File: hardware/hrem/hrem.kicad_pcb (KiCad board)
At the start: 2 copper layers, 88.9 x 53.3 mm, 18 parts, among them J1 ICSP, J2 Hall_Conn, Q1 BC547, SW1 SW_Push_Dual, U1 HT7733A, U2 ATtiny85

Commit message: Update ICSP footprint information
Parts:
- J1: footprint Connector_PinSocket_2.54mm:PinSocket_2x05_P2.54mm_Vertical -> Connector_IDC:IDC-Header_2x05_P2.54mm_Vertical
- moved J1 5.68 mm to (63.5, 66.0)
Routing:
- net GND: track 207.6 -> 168.1 mm
- net /MOSI: track 25.5 -> 0.06 mm, vias 2 -> 0
- net /SCK: track 40.6 -> 25.4 mm
- net /MISO: track 35.6 -> 22.9 mm
- net /RST: track 10.2 -> 0.00 mm
- net VCC: track 61.0 -> 58.4 mm

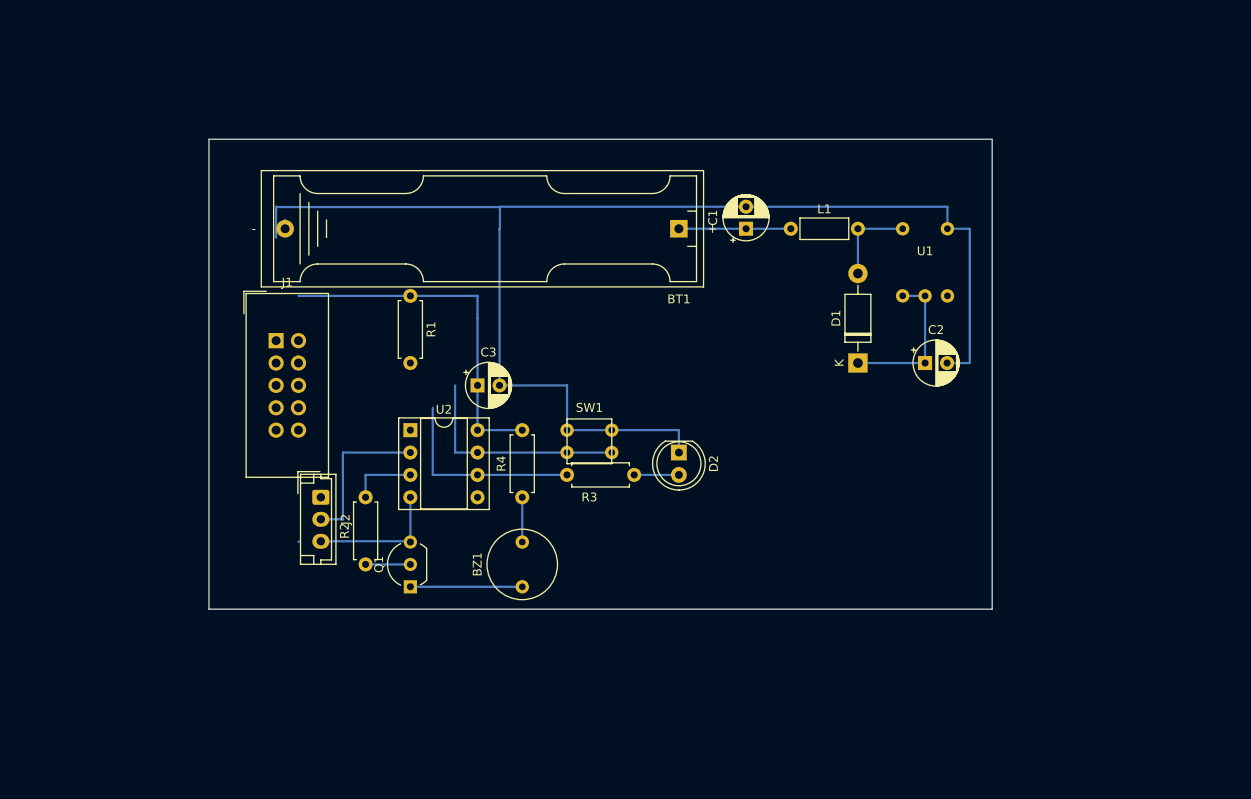
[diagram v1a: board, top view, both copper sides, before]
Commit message: KiCad new footprints
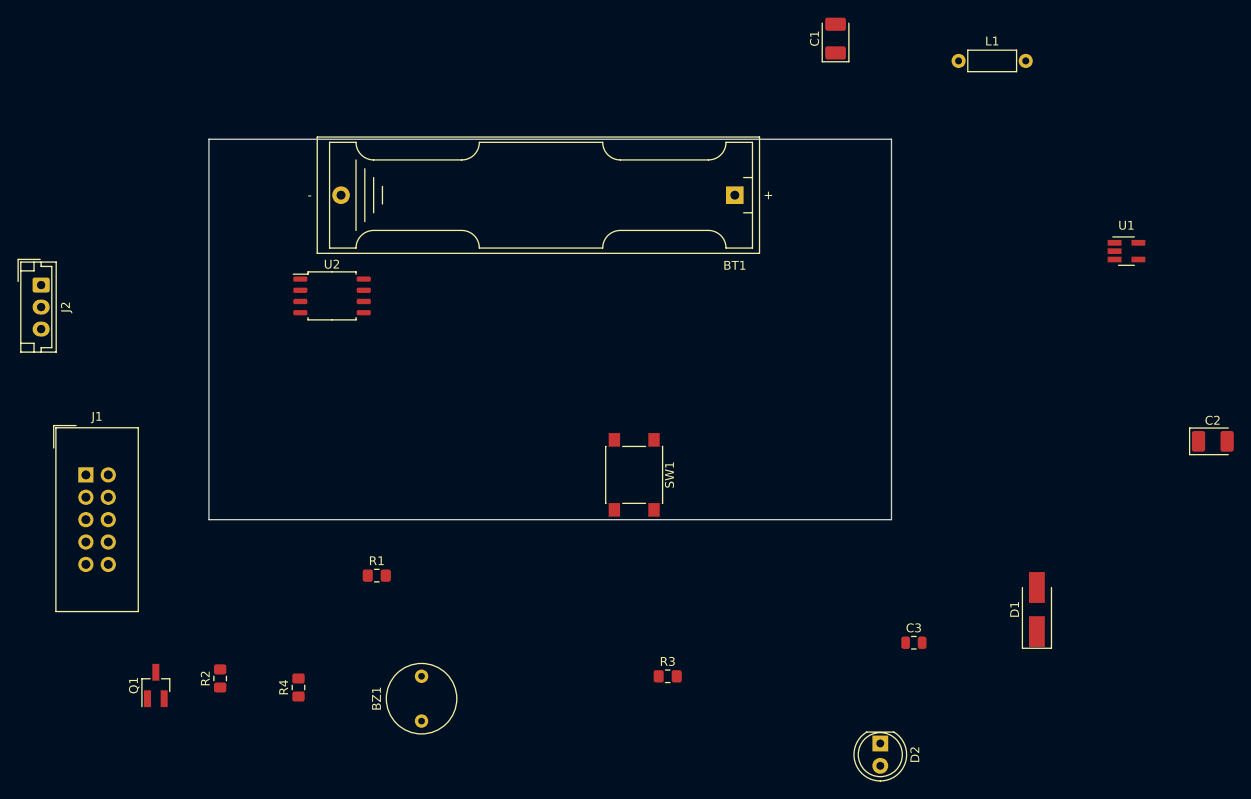
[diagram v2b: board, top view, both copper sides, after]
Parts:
- C1, C2: footprint Capacitor_THT:CP_Radial_D5.0mm_P2.50mm -> Capacitor_Tantalum_SMD:CP_EIA-3528-15_AVX-H_Pad1.50x2.35mm_HandSolder
- C3: footprint Capacitor_THT:CP_Radial_D5.0mm_P2.50mm -> Capacitor_SMD:C_0805_2012Metric
- D1: value 1N5817 -> SS14-E3/61T; footprint Diode_THT:D_DO-41_SOD81_P10.16mm_Horizontal -> Diode_SMD:D_SMA_Handsoldering
- Q1: value BC547 -> MMBT4401-7-F; footprint Package_TO_SOT_THT:TO-92_Inline_Wide -> Package_TO_SOT_SMD:SOT-23_Handsoldering
- R1, R2, R3, R4: footprint Resistor_THT:R_Axial_DIN0207_L6.3mm_D2.5mm_P7.62mm_Horizontal -> Resistor_SMD:R_0805_2012Metric_Pad1.15x1.40mm_HandSolder
- SW1: footprint hrem:button -> Button_Switch_SMD:SW_Push_1P1T_NO_6x6mm_H9.5mm
- U1: footprint hrem:HT7733 -> Package_TO_SOT_SMD:SOT-23-5_HandSoldering
- U2: footprint Package_DIP:DIP-8_W7.62mm_Socket -> Package_SO:SOIC-8_5.23x5.23mm_P1.27mm
- moved C3 57.5 mm to (135.9, 100.3)
- moved D2 40.2 mm to (132.1, 111.8)
- moved J2 39.9 mm to (36.8, 59.7)
- moved D1 34.6 mm to (149.9, 96.6)
- moved C2 33.9 mm to (169.8, 77.5)
- moved R4 33.3 mm to (66.0, 105.4)
- moved R1 32.0 mm to (74.9, 92.7), turned to 0 degrees
- moved Q1 31.0 mm to (49.9, 105.2)
- moved L1 26.9 mm to (141.0, 34.3)
- moved J1 26.4 mm to (41.9, 81.3)
- moved R3 25.6 mm to (108.0, 104.1)
- moved C1 23.9 mm to (127.0, 31.8)
- moved U1 23.4 mm to (160.0, 55.9)
- moved R2 21.0 mm to (57.1, 104.4)
- moved BZ1 19.1 mm to (80.0, 106.7)
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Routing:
- net GND: track 168.1 -> 0.00 mm
- net VCC: track 58.4 -> 0.00 mm
- net /SCK: track 25.4 -> 0.00 mm
- net /MISO: track 22.9 -> 0.00 mm
- net Net-(J2-Pad2): track 17.8 -> 0.00 mm
- net Net-(BZ1-Pad2): track 12.7 -> 0.00 mm
- net Net-(BT1-Pad1): track 12.7 -> 0.00 mm
- net Net-(D1-Pad2): track 10.2 -> 0.00 mm
- net Net-(R2-Pad2): track 7.62 -> 0.00 mm
- net Net-(BZ1-Pad1): track 5.08 -> 0.00 mm
- net Net-(Q1-Pad2): track 5.08 -> 0.00 mm
- net Net-(D2-Pad2): track 5.08 -> 0.00 mm
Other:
- board size 88.9 x 53.3 mm -> 77.5 x 43.2 mm

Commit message: Work over schematics
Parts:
- added R5: 0R, Resistor_SMD:R_0805_2012Metric_Pad1.15x1.40mm_HandSolder, F.Cu at (128.5, 61.0)
- added R6: 0R, Resistor_SMD:R_0805_2012Metric_Pad1.15x1.40mm_HandSolder, F.Cu at (123.2, 60.3)
- added REF**: KiCad-Logo2_5mm_SilkScreen, Symbol:KiCad-Logo2_5mm_SilkScreen, F.Cu at (69.2, 80.6)
- added REF**: MountingHole_3mm, MountingHole:MountingHole_3mm, F.Cu at (132.3, 46.4)
- added REF**: MountingHole_3mm, MountingHole:MountingHole_3mm, F.Cu at (132.3, 84.4)
- added REF**: MountingHole_3mm, MountingHole:MountingHole_3mm, F.Cu at (59.3, 84.4)
- added REF**: MountingHole_3mm, MountingHole:MountingHole_3mm, F.Cu at (59.3, 46.4)
- added TP1: TestPoint_Flag, TestPoint:TestPoint_Loop_D2.50mm_Drill1.0mm, F.Cu at (132.7, 57.8)
- added TP2: TestPoint_Flag, TestPoint:TestPoint_Pad_D2.0mm, F.Cu at (59.7, 77.5)
- added TP3: TestPoint_Flag, TestPoint:TestPoint_Pad_D2.0mm, F.Cu at (116.2, 72.4)
- added TP4: TestPoint_Flag, TestPoint:TestPoint_Pad_D2.0mm, F.Cu at (114.3, 83.8)
- added TP5: TestPoint_Flag, TestPoint:TestPoint_Pad_D2.0mm, F.Cu at (101.0, 81.9)
- added U3: 74LVC1G125, Package_TO_SOT_SMD:SOT-23-5_HandSoldering, F.Cu at (126.4, 70.5)
- added U4: 74LVC1G125, Package_TO_SOT_SMD:SOT-23-5_HandSoldering, F.Cu at (115.0, 62.9)
- BT1: footprint Battery:BatteryHolder_Keystone_2466_1xAAA -> hrem:AAA battery
- BZ1, SW1: moved to B.Cu
- C3: footprint Capacitor_SMD:C_0805_2012Metric -> Capacitor_SMD:C_0805_2012Metric_Pad1.15x1.40mm_HandSolder
- D2: footprint LED_THT:LED_D5.0mm -> LED_THT:LED_D3.0mm; moved to B.Cu
- J1: value ICSP -> AVR-ISP
- L1: footprint Inductor_THT:L_Axial_L5.3mm_D2.2mm_P7.62mm_Horizontal_Vishay_IM-1 -> hrem:Murata LQH43
- moved C2 99.8 mm to (71.1, 62.9)
- moved D1 95.6 mm to (59.1, 66.6)
- moved U1 94.7 mm to (66.0, 67.3)
- moved J2 88.7 mm to (123.8, 76.9)
- moved L1 82.5 mm to (62.2, 59.1)
- moved R2 81.4 mm to (127.9, 64.1), turned to 180 degrees
- moved C1 74.0 mm to (66.0, 73.7), turned to 180 degrees
- moved D2 61.3 mm to (92.7, 64.8), turned to 90 degrees
- moved R4 55.6 mm to (114.1, 77.5), turned to 0 degrees
- moved Q1 50.1 mm to (88.3, 73.0)
- moved BZ1 47.1 mm to (101.6, 64.8), turned to 90 degrees
- moved R1 41.4 mm to (114.3, 80.0)
- moved J1 40.7 mm to (82.5, 83.2), turned to 90 degrees
- moved R3 36.9 mm to (110.7, 67.3)
- moved U2 35.9 mm to (102.9, 74.9)
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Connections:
- net Net-(BT1-Pad1) renamed /Vbat
- J2 pad 1: /MOSI -> Net-(J2-Pad1)
- R3 pad 1: /MISO -> Net-(R3-Pad1)
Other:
- board size 77.5 x 43.2 mm -> 80 x 44.4 mm

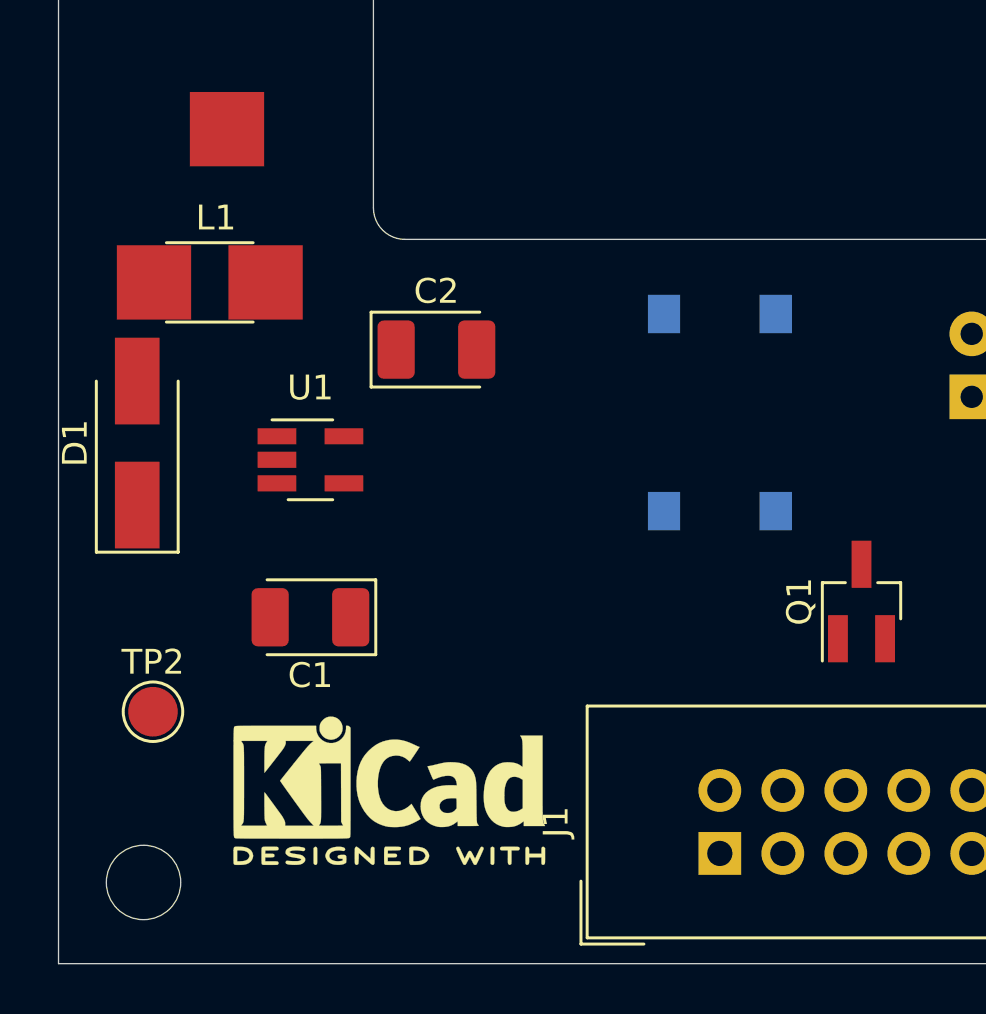
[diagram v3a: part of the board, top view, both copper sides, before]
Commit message: Button footprint added
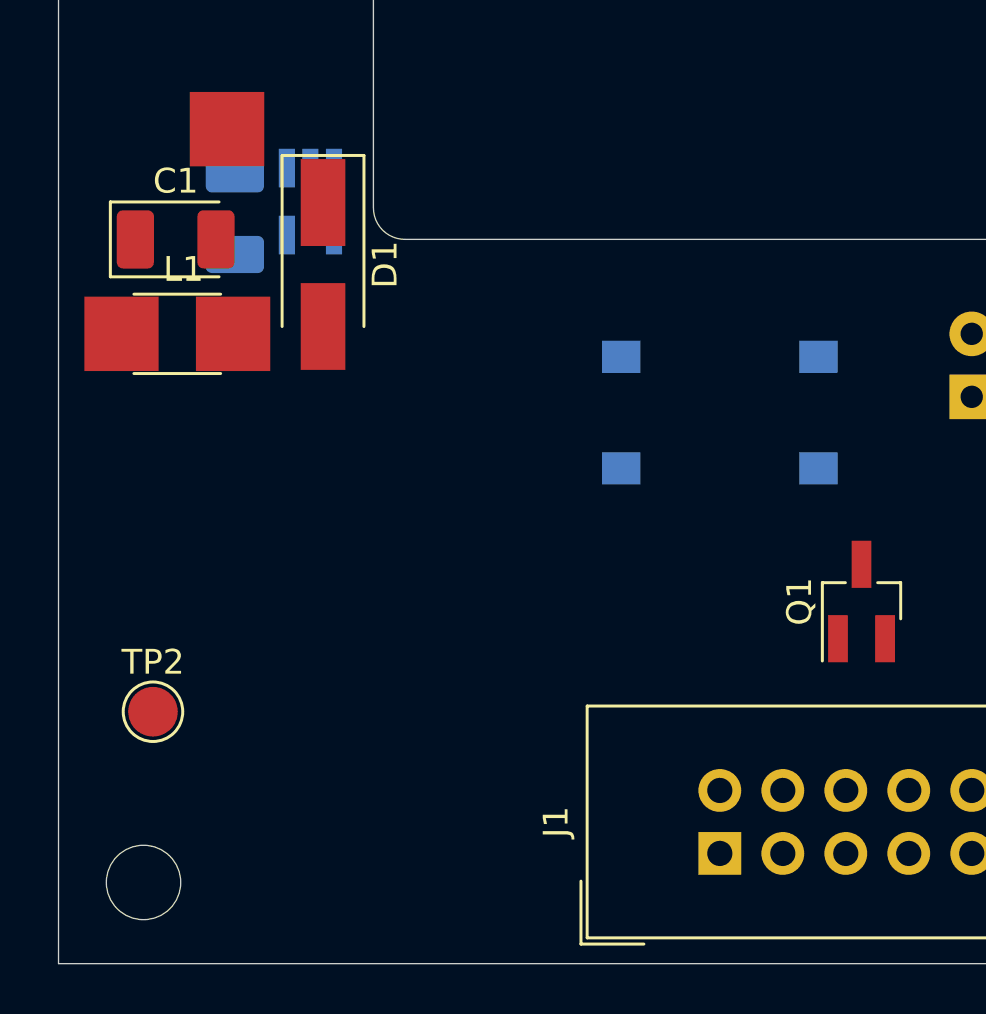
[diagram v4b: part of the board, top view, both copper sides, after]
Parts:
- removed the REF** at (69.2, 80.6)
- C2, U1: moved to B.Cu
- SW1: footprint Button_Switch_SMD:SW_Push_1P1T_NO_6x6mm_H9.5mm -> hrem:Diptronics DTSM-65N
- moved C1 16.2 mm to (60.6, 58.4), turned to 0 degrees
- moved U1 10.4 mm to (66.0, 56.9), turned to 270 degrees
- moved D1 10.4 mm to (66.5, 59.4), turned to 270 degrees
- moved C2 9.79 mm to (63.0, 57.4), turned to 270 degrees
- moved L1 2.45 mm to (60.9, 61.1)
- turned SW1 to 0 degrees
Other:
- net class POWER added: clearance 0.2, trace_width 1, via_dia 0.8, via_drill 0.4

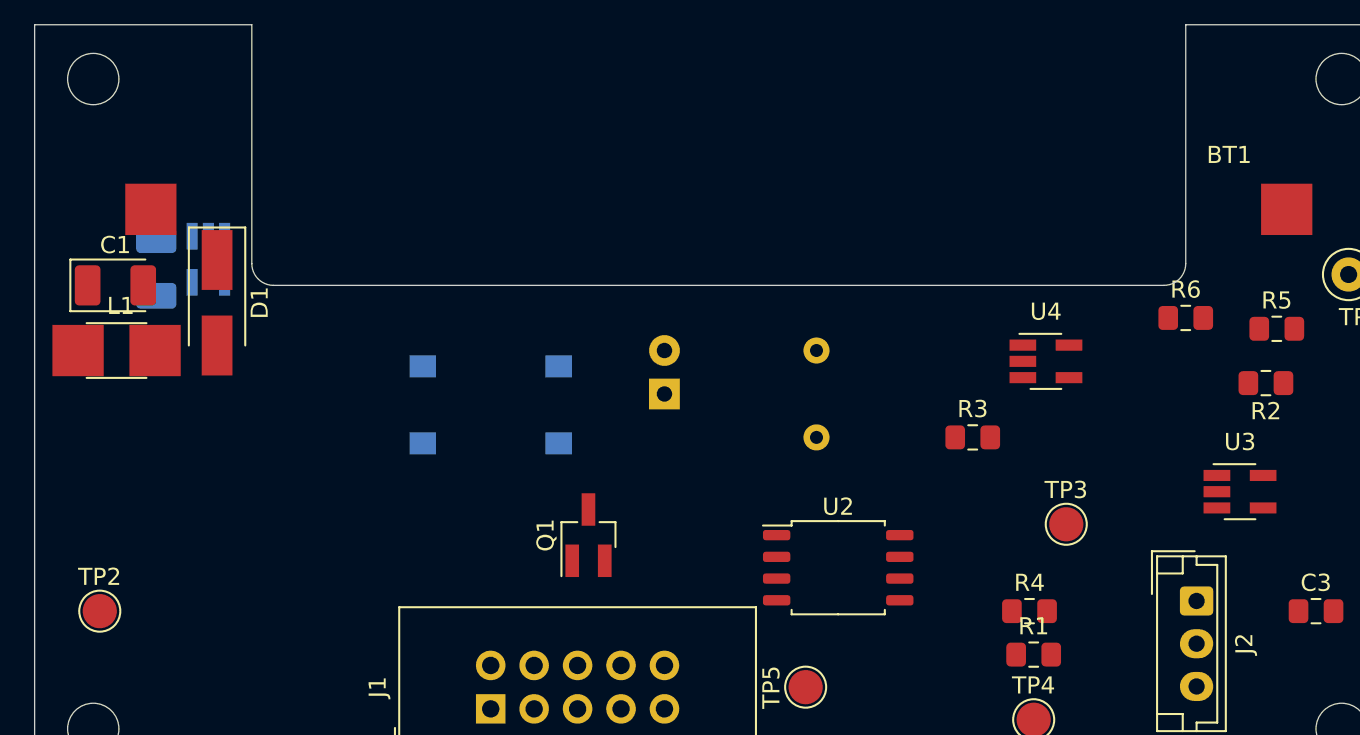
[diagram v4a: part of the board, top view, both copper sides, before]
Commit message: Boosting voltage regulator pcb layout
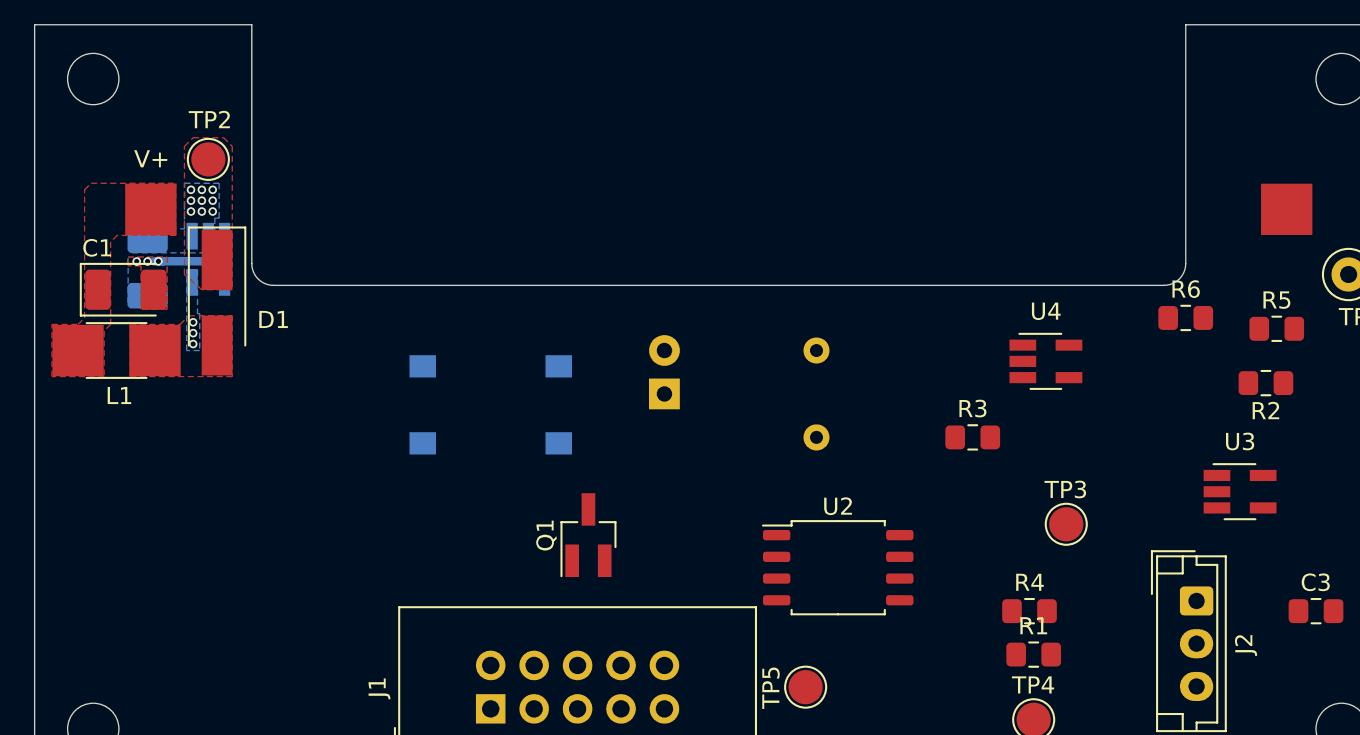
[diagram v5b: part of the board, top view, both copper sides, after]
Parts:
- moved TP2 27.2 mm to (66.0, 51.1)
- moved C1 0.66 mm to (61.2, 58.7)
- moved C2 0.51 mm to (62.5, 57.4)
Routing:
- net GND: track 0.00 -> 5.61 mm, vias 0 -> 3
- net VCC: vias 0 -> 9
- net Net-(D1-Pad2): vias 0 -> 3
- added copper zone on F.Cu, net /Vbat
- added copper zone on B.Cu, net GND
- added copper zone on F.Cu, net GND
- added copper zone on B.Cu, net Net-(D1-Pad2)
- added copper zone on F.Cu, net Net-(D1-Pad2)
- added copper zone on B.Cu, net VCC
- added copper zone on F.Cu, net VCC
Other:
- net class Default: via_dia 0.8 -> 0.5; via_drill 0.4 -> 0.3
- net class POWER: trace_width 1 -> 0.5; via_dia 0.8 -> 0.5; via_drill 0.4 -> 0.3
- rule via_min_drill: 0.3 -> 0.2
- rule via_min_size: 0.4 -> 0.45
- board text added: "V+"

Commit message: Buzzer and LED PCB layout
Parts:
- C3, R1, U3: moved to B.Cu
- moved R2 31.5 mm to (96.5, 67.2), turned to 270 degrees
- moved C3 31.5 mm to (99.4, 74.7), turned to 270 degrees
- moved D2 23.8 mm to (116.5, 64.2)
- moved TP3 23.3 mm to (93.7, 66.2)
- moved TP5 22.5 mm to (122.4, 75.3)
- moved R1 19.2 mm to (96.1, 73.7), turned to 180 degrees
- moved R5 17.3 mm to (118.7, 75.2)
- moved U3 16.3 mm to (111.6, 63.6), turned to 90 degrees
- moved R4 15.5 mm to (102.6, 67.1), turned to 270 degrees
- moved Q1 13.6 mm to (98.0, 63.6), turned to 0 degrees
- moved R6 12.3 mm to (111.7, 64.7), turned to 90 degrees
- moved U4 11.0 mm to (121.2, 72.0)
- moved TP4 9.28 mm to (122.3, 79.1)
- moved R3 5.99 mm to (112.7, 61.7)
- moved U2 4.56 mm to (98.3, 75.4)
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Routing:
- net GND: track 5.61 -> 15.6 mm, vias 3 -> 6
- net Net-(BZ1-Pad2): track 0.00 -> 4.32 mm
- net /MISO: track 0.00 -> 2.94 mm, vias 0 -> 1
- net Net-(D2-Pad2): track 0.00 -> 2.78 mm
- net Net-(R3-Pad1): vias 0 -> 2
- added copper zone on F.Cu, net Net-(Q1-Pad2)
- added copper zone on B.Cu, net Net-(R3-Pad1)
- added copper zone on F.Cu, net Net-(R3-Pad1)

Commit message: Work on PCB layout
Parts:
- J2: footprint Connector_JST:JST_EH_B3B-EH-A_1x03_P2.50mm_Vertical -> hrem:X8821WRS-03-9TSN
- R5, U4: moved to B.Cu
- moved TP4 14.4 mm to (130.5, 67.3)
- moved J1 10.9 mm to (69.8, 77.0), turned to 90 degrees
- moved TP5 8.89 mm to (126.3, 67.3), turned to 180 degrees
- moved U4 5.93 mm to (124.3, 77.0), turned to 180 degrees
- moved C3 4.07 mm to (97.8, 78.4), turned to 180 degrees
- moved TP1 3.84 mm to (129.0, 58.9)
- moved R1 3.34 mm to (97.9, 76.5)
- moved U2 3.27 mm to (97.9, 78.7)
- moved R5 2.38 mm to (120.3, 77.0), turned to 270 degrees
- moved D2 1.17 mm to (117.3, 65.1)
- moved R3 1.17 mm to (113.5, 62.5)
- moved R6 1.17 mm to (112.5, 65.6)
- moved U3 1.17 mm to (112.4, 64.5)
- moved J2 1.16 mm to (125.7, 75.4)
- moved SW1 0.93 mm to (82.4, 64.5)
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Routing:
- net /MOSI: track 0.00 -> 61.9 mm, vias 0 -> 3
- net Net-(J2-Pad2): track 0.00 -> 57.3 mm
- net /SCK: track 0.00 -> 55.8 mm, vias 0 -> 2
- net GND: track 15.6 -> 64.0 mm, vias 6 -> 13
- net /MISO: track 2.94 -> 44.8 mm, vias 1 -> 3
- net /RST: track 0.00 -> 23.1 mm, vias 0 -> 3
- net Net-(J2-Pad1): track 0.00 -> 22.9 mm, vias 0 -> 1
- net Net-(R2-Pad2): track 0.00 -> 15.3 mm
- net Net-(BZ1-Pad1): track 0.00 -> 2.79 mm
- net VCC: vias 9 -> 13
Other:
- board text removed: "V+"

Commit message: PCB layout all set
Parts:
- moved TP1 5.83 mm to (124.5, 62.5)
- moved TP2 1.73 mm to (64.6, 50.0)
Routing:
- net VCC: track 0.00 -> 42.5 mm, vias 13 -> 15
- net GND: track 64.0 -> 44.2 mm, vias 13 -> 23
- net /MISO: track 44.8 -> 48.9 mm, vias 3 -> 2
- net /SCK: track 55.8 -> 52.4 mm
- net Net-(Q1-Pad2): track 0.00 -> 2.79 mm
- net Net-(J2-Pad2): track 57.3 -> 54.7 mm
- net /RST: track 23.1 -> 25.6 mm, vias 3 -> 1
- net Net-(R2-Pad2): track 15.3 -> 13.7 mm
- net /MOSI: track 61.9 -> 60.8 mm, vias 3 -> 1
